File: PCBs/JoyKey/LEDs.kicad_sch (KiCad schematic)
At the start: 11 parts, among them J2 Conn_01x03_Socket

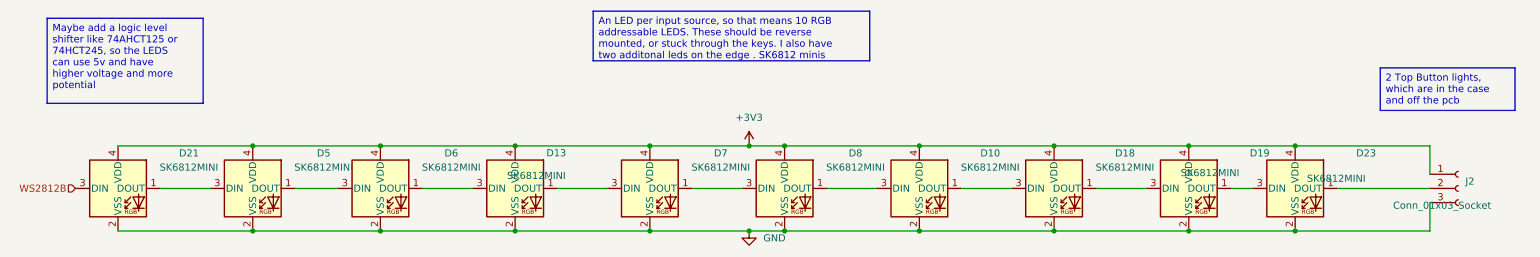
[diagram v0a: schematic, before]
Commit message: Add decoupling capacitors to LEDs
There isn't much to loose from this
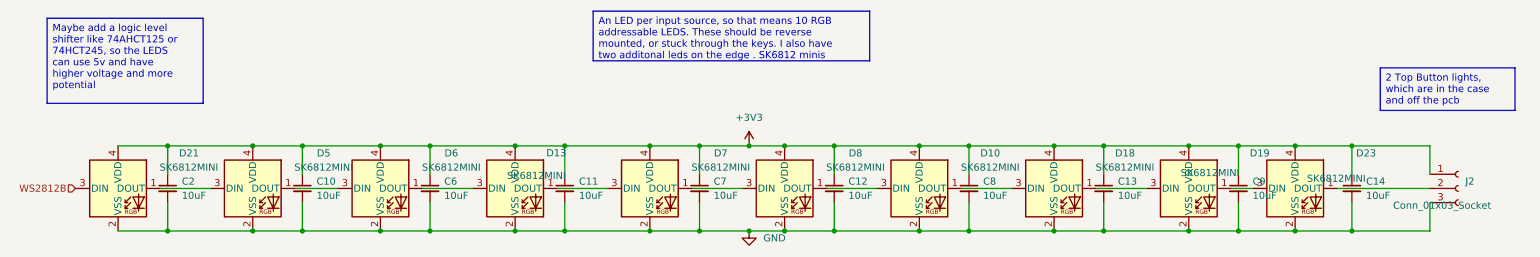
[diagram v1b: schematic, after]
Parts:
- added C10, C11, C12, C13, C14, C2, C6, C7, C8, C9: 10uF, Capacitor_SMD:C_0805_2012Metric, symbol Device:C_Small
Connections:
- net +3V3: now also C10.1, C11.1, C12.1, C13.1, C14.1, C2.1, C6.1, C7.1, C8.1, C9.1
- net GND: now also C10.2, C11.2, C12.2, C13.2, C14.2, C2.2, C6.2, C7.2, C8.2, C9.2
